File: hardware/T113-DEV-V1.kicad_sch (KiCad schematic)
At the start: 0 parts

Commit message: 電源頁開畫:RY1303 輸入側、EN1 延遲 RC 完成
- 根圖紙掛上階層式子頁 power.kicad_sch(p.2 電源)
- 電源頁小顆 IC 符號由 gen_power_symbols.py 生成(RY1303 / APX803 / TPS2051B)
- RY1303:VIN1~3、EN2/EN3 → +5V_VBUS,各 VIN 10uF 並聯到地;8 支地腳含 EP → GND
- EN1:47K 上拉 +3V3 + 220nF 到地(T1 ≈ 4.67 ms)
- 下一步:三路輸出(SW → L → C_out,FB 分壓),先做 CH3 +3V3
- ROADMAP 補第 4 塊 RK3568;reference 補 APX803 / TPS2051B 資料來源
- .gitignore 排除 KiCad 10 的 .history/

Co-Authored-By: Claude Opus 5.5 <noreply@anthropic.com>
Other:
- added sheet 電源 (power.kicad_sch)
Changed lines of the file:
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@@
 (kicad_sch
-	(version 20250114)
+	(version 20260306)
 	(generator "eeschema")
 	(generator_version "10.0")
@@
 		(comment 1 "根目錄圖紙 —— 各介面分頁掛在這裡")
 	)
+	(sheet
+		(at 33.02 39.37)
+		(size 93.98 54.61)
+		(exclude_from_sim no)
+		(in_bom yes)
+		(on_board yes)
+		(dnp no)
+		(fields_autoplaced yes)
+		(stroke
+			(width 0.1524)
+			(type solid)
+		)
+		(fill
+			(color 0 0 0 0)
+		)
+		(property "Sheetname" "電源"
+			(at 33.02 38.6584 0)
+			(show_name no)
+			(do_not_autoplace no)
+			(effects
+				(font
+					(size 1.27 1.27)
+				)
+				(justify left bottom)
+			)
+		)
+		(property "Sheetfile" "power.kicad_sch"
+			(at 33.02 94.5646 0)
+			(show_name no)
+			(do_not_autoplace no)
+			(effects
+				(font
+					(size 1.27 1.27)
+				)
+				(justify left top)
+			)
+		)
+		(instances
+			(project "T113-DEV-V1"
+				(path "/00000000-0000-0000-0000-000000000001"
+					(page "2")
+				)
+			)
+		)
+	)
 	(sheet_instances
-		(path "/" (page "1"))
+		(path "/"
+			(page "1")
+		)
 	)
+	(embedded_fonts no)
 )

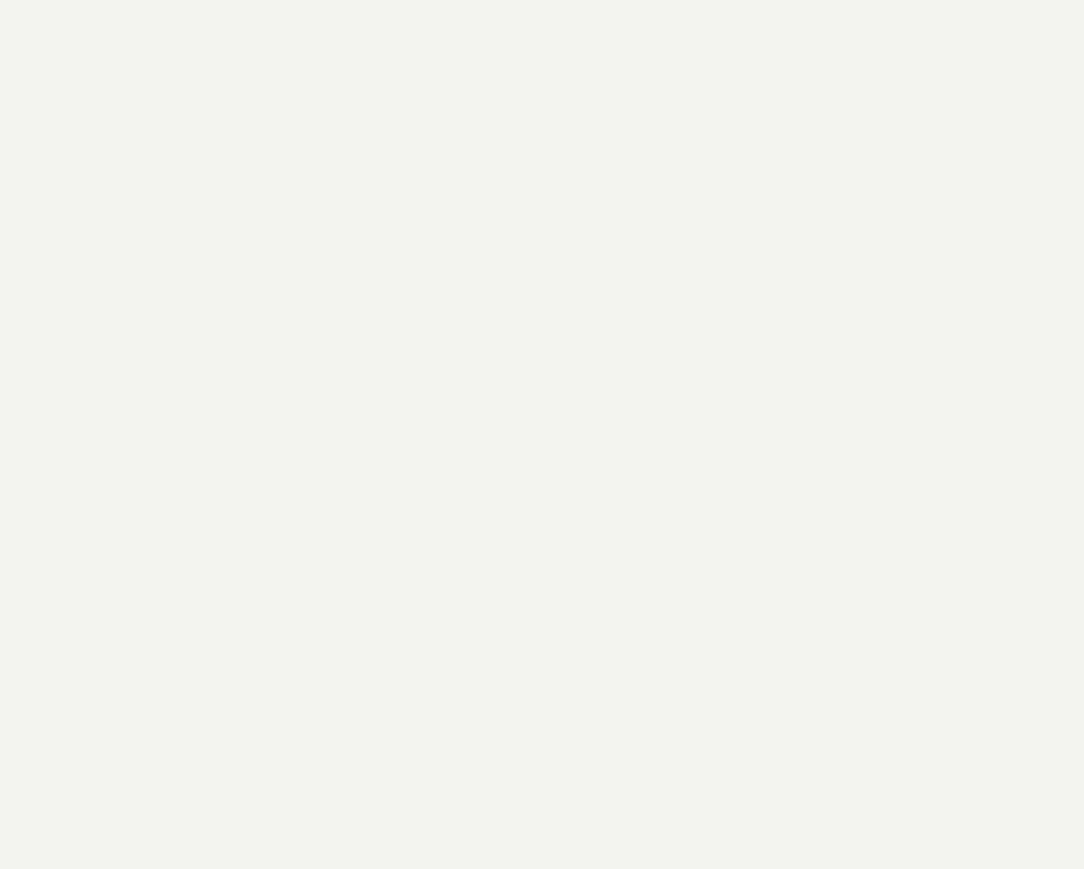
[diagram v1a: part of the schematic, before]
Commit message: 主晶片頁開工:unit 1(26 支電源腳)完成
建立 mcu.kicad_sch 並掛進階層,U6 = T113-S3。

供電骨架:
  +0V9       VDD-CORE0/1、VDD-SYS0/1/2
  +1V5       VCC-DRAM0/1
  +3V3       VCC-IO/PD/PE/PG/TVOUT、LDO-IN
  +1V8_SOC   VCC-PLL/RTC/LVDS、VDD18-DRAM、VCC-TVIN
  +1V8_AUDIO LDOA-OUT、AVCC、HPVCC
  GND        AGND、EPAD
  獨立 net   LDOB-OUT(C17 2.2uF)、VRA1(C18 0.1uF)、VRA2(C19 0.1uF)

★ 三個「輸出型」腳位不可接電源軌:
  LDOA-OUT   內建 LDO 輸出 → 只接 +1V8_AUDIO
  LDOB-OUT   不使用 → 只掛電容到地
  VRA1/VRA2  Internal Reference Voltage,Type = AO → 只掛電容到地
  接到軌上就是兩個源打架(同電源頁踩過的 U3 VOUT 並聯到 U2 輸出)。

查 Type 欄比查名稱可靠 —— LDOA-OUT 名字看得出方向,
VRA1/VRA2 完全看不出來,只有 Table 4-4 (p.45) 的 AO 說得準。

待確認:VRA1/VRA2 去耦值暫用 0.1uF,DS 無建議值,要對 MangoPi 原理圖。

Co-Authored-By: Claude Opus 5 <noreply@anthropic.com>
Claude-Session: https://claude.ai/code/session_01HtGUWSQFey6W2g2grqgTMR
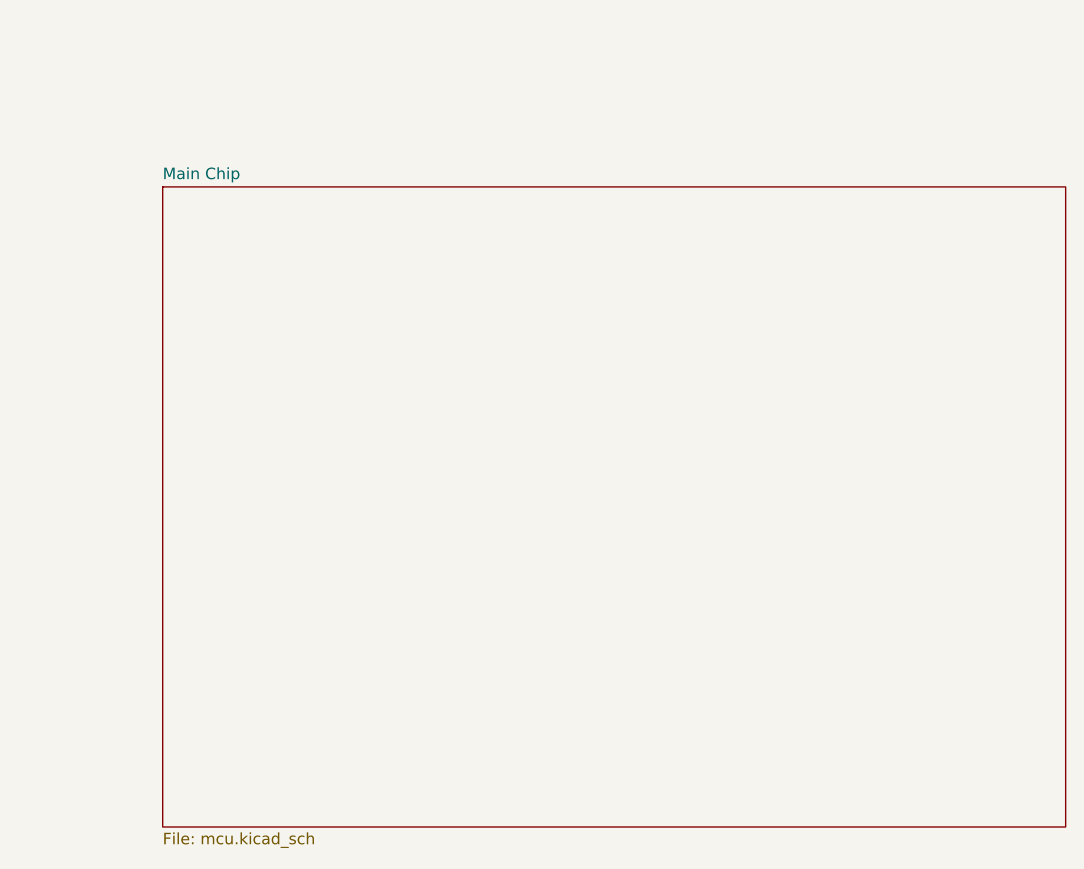
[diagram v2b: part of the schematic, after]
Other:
- added sheet Main Chip (mcu.kicad_sch)
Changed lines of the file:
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@@
+		)
+	)
+	(sheet
+		(at 57.658 134.112)
+		(size 100.33 71.12)
+		(exclude_from_sim no)
+		(in_bom yes)
+		(on_board yes)
+		(dnp no)
+		(fields_autoplaced yes)
+		(stroke
+			(width 0.1524)
+			(type solid)
+		)
+		(fill
+			(color 0 0 0 0)
+		)
+		(property "Sheetname" "Main Chip"
+			(at 57.658 133.4004 0)
+			(show_name no)
+			(do_not_autoplace no)
+			(effects
+				(font
+					(size 1.27 1.27)
+				)
+				(justify left bottom)
+			)
+		)
+		(property "Sheetfile" "mcu.kicad_sch"
+			(at 57.658 205.8166 0)
+			(show_name no)
+			(do_not_autoplace no)
+			(effects
+				(font
+					(size 1.27 1.27)
+				)
+				(justify left top)
+			)
+		)
+		(instances
+			(project "T113-DEV-V1"
+				(path "/00000000-0000-0000-0000-000000000001"
+					(page "3")
+				)
+			)
 		)
 	)

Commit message: 原理圖十一頁全部寫進專案,ERC 歸零
關掉 KiCad 之後執行 run_all.py --apply,23 步全過。

關閉前先確認過未存檔的修改是什麼:
  KiCad 標題有 * 標記,但比對 .history(KiCad 自己的 autosave repo)
  與 HEAD 的差異只有 10 行,而且全是視覺層面 ——
  一條裝飾用分隔線的端點差 0.76mm、一顆 GND 符號的文字標籤位置。
  沒有任何元件、接線、net 名稱、腳位的改變。
  而且 .history 那份(15:50 autosave)比 HEAD(15:51 commit)還舊,
  磁碟上的就是最新版。沒有東西遺失。

寫進專案的內容
  新增 8 張子頁:display / hdmi / mipi / net / usb / storage / header / audio
  mcu 頁補 unit 6/7 接線、兩顆晶振、23 顆逐腳去耦
  power 頁補 4 個 PWR_FLAG
  修掉手畫頁殘留:兩段 1.27mm 殘線、AGND 線尾沒放接地符號、
  排針串接電阻與兩顆 IC 的 footprint
  PG12/PG14/PG4 改名為 HDMI_INT_N / HDMI_PD / PANEL_RESET_N
  產生 T113-S3 的 eLQFP128 footprint(內建件 + EPAD + thermal via)

驗證(真實專案,非副本)
  ERC                0 errors · 0 warnings
  check_schematic    0 errors · 0 warnings
  check_power_rails  全部通過
  209 顆元件 · 253 條 net · 11 頁 · 缺 footprint 0

接下來是 PCB layout,那是使用者的部分。

Co-Authored-By: Claude Opus 5 <noreply@anthropic.com>
Claude-Session: https://claude.ai/code/session_01HtGUWSQFey6W2g2grqgTMR
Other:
- added sheet USB 與開機 (usb.kicad_sch)
- added sheet 儲存 (storage.kicad_sch)
- added sheet 排針 (header.kicad_sch)
- added sheet 網路 (net.kicad_sch)
- added sheet 音訊 (audio.kicad_sch)
- added sheet 顯示 · ADV7511 (display.kicad_sch)
- added sheet 顯示 · HDMI 座 (hdmi.kicad_sch)
- added sheet 顯示 · MIPI DSI (mipi.kicad_sch)
